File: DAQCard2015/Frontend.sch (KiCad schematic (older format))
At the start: 12 parts, among them P7 CONN_02X20_Double, U1 RJ45x8, U2 AD5628

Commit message: Adds APC128 connections and voltage supplies
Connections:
- net ADC_SCLK is gone; now on net SPI_SCLK: U2.16 (SCLK)
- net ADC_SDIO is gone; now on net SPI_SDIO: U2.15 (DIN)
- net Aref renamed Aref_A
- net Aref_A: no longer P7.74 (P34)
- net RBO1 renamed RBO_A1
- net RBO2 renamed RBO_A2
- net RBO3 renamed RBO_A3
- net RBO4 renamed RBO_A4
- net RBO5 renamed RBO_B1
- net RBO6 renamed RBO_B2
- net RBO7 renamed RBO_B3
- net RBO8 renamed RBO_B4
- net RG renamed RG_A
- net RG_A: no longer P7.56 (P16)
- net Vana renamed Vana_A
- net Vana_A: no longer P7.44 (P4), P7.45 (P5)
- new net Aref_B: P7.74 (P34)
- new net RG_B: P7.56 (P16)
- new net Vana_B: P7.44 (P4), P7.45 (P5)
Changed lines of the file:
@@
 	1    0    0    -1
 $EndComp
-Text GLabel 19750 4150 1    60   Input ~ 0
+Text GLabel 19750 4150 1    40   Input ~ 0
 GND
 Wire Wire Line
@@
 Wire Wire Line
 	19400 4650 19900 4650
-Text GLabel 19400 4650 0    60   Input ~ 0
+Text GLabel 19400 4650 0    40   Input ~ 0
 3V3dig
 Wire Wire Line
@@
 F28 "Vocm" I T 7600 3250 60
 $EndSheet
-Text HLabel 21000 4550 2    60   Input ~ 0
-ADC_SDIO
-Text HLabel 21000 4450 2    60   Input ~ 0
-ADC_SCLK
 $Sheet
 S 3750 7050 3400 1050
@@
 Text GLabel 3200 7700 1    40   Input ~ 0
 ADC_CLK-
-Text GLabel 19550 4550 1    60   Input ~ 0
+Text GLabel 19550 4550 1    40   Input ~ 0
 RNGDAC_CSB
 Text GLabel 7700 10350 2    40   Input ~ 0
-Vana
+Vana_A
 Text GLabel 7700 10450 2    40   Input ~ 0
 Vdig
@@
 CS
 Text GLabel 7700 10950 2    40   Input ~ 0
-RG
+RG_A
 Text GLabel 7700 11050 2    40   Input ~ 0
 IS2
@@
 SEB
 Text GLabel 7700 11550 2    40   Input ~ 0
-RBO1
+RBO_A1
 Text GLabel 7700 11650 2    40   Input ~ 0
-RBO3
+RBO_A3
 Text GLabel 7700 11750 2    40   Input ~ 0
 RPHI2
 Text GLabel 7700 11850 2    40   Input ~ 0
-Aref
+Aref_A
 Text GLabel 7700 10650 2    40   Input ~ 0
 5Vdig
@@
 RPHI1
 Text GLabel 7200 11750 0    40   Input ~ 0
-RBO4
+RBO_A4
 Text GLabel 7200 11650 0    40   Input ~ 0
-RBO2
+RBO_A2
 Text GLabel 7200 11450 0    40   Input ~ 0
 SBI
@@
 Vdig
 Text GLabel 7200 10450 0    40   Input ~ 0
-Vana
+Vana_A
 Text GLabel 7200 10250 0    40   Input ~ 0
 Vbias
@@
 RPHI1
 Text GLabel 8250 11750 0    40   Input ~ 0
-RBO8
+RBO_B4
 Text GLabel 8250 11650 0    40   Input ~ 0
-RBO6
+RBO_B2
 Text GLabel 8250 11450 0    40   Input ~ 0
 SBI
@@
 Vdig
 Text GLabel 8250 10450 0    40   Input ~ 0
-Vana
+Vana_B
 Text GLabel 8250 10250 0    40   Input ~ 0
 Vbias
@@
 SDA
 Text GLabel 8750 10350 2    40   Input ~ 0
-Vana
+Vana_B
 Text GLabel 8750 10450 2    40   Input ~ 0
 Vdig
@@
 CS
 Text GLabel 8750 10950 2    40   Input ~ 0
-RG
+RG_B
 Text GLabel 8750 11050 2    40   Input ~ 0
 IS2
@@
 SEB
 Text GLabel 8750 11550 2    40   Input ~ 0
-RBO5
+RBO_B1
 Text GLabel 8750 11650 2    40   Input ~ 0
-RBO7
+RBO_B3
 Text GLabel 8750 11750 2    40   Input ~ 0
 RPHI2
 Text GLabel 8750 11850 2    40   Input ~ 0
-Aref
+Aref_B
 Text GLabel 8750 10650 2    40   Input ~ 0
 5Vdig
 Text GLabel 8750 12050 2    40   Input ~ 0
 SCL
+Text GLabel 21000 4450 2    40   Input ~ 0
+SPI_SCLK
+Text GLabel 21000 4550 2    40   Input ~ 0
+SPI_SDIO
 $EndSCHEMATC

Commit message: Update to DAQ Board including adding an JTAG header and hooking up external clock and trigger
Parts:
- added C59, C61, C62, C63: 10uF, Capacitors_SMD:C_0805, symbol C
- added C78: .1uF, Capacitors_SMD:C_0603, symbol C
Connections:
- net 3V3ana: now also C59.1, C61.1, C62.1, C63.1
- net 3V3dig: now also C78.1
- net GND: now also C59.2, C61.2, C62.2, C63.2, C78.2
- net Vocm: no longer P7.48 (P8), P7.49 (P9), P7.8 (P8), P7.9 (P9)
- net Vdig renamed 2V5dig
- new net Vocm_tel: P7.48 (P8), P7.49 (P9), P7.8 (P8), P7.9 (P9)
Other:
- note added: "Amplifier Decoupling Caps"
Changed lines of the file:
@@
 	1    0    0    -1
 $EndComp
-Text GLabel 19750 4150 1    40   Input ~ 0
+Text GLabel 19750 4050 1    40   Input ~ 0
 GND
 Wire Wire Line
-	19900 4550 19550 4550
+	19900 4550 19600 4550
 Wire Wire Line
 	19750 4450 19900 4450
 Wire Wire Line
-	19750 4150 19750 4450
+	19750 4050 19750 4450
 Wire Wire Line
 	21000 4650 21500 4650
 Wire Wire Line
-	21500 5500 21500 4200
-Wire Wire Line
-	21500 4200 19750 4200
-Connection ~ 19750 4200
-Wire Wire Line
-	19400 4650 19900 4650
-Text GLabel 19400 4650 0    40   Input ~ 0
+	21500 4100 21500 5500
+Connection ~ 19750 4100
+Wire Wire Line
+	19250 4650 19900 4650
+Text GLabel 19250 4650 0    40   Input ~ 0
 3V3dig
 Wire Wire Line
@@
 $EndComp
 Wire Wire Line
-	20300 5500 21500 5500
+	21500 5500 20300 5500
 Connection ~ 21500 5150
 $Comp
@@
 Text GLabel 3200 7700 1    40   Input ~ 0
 ADC_CLK-
-Text GLabel 19550 4550 1    40   Input ~ 0
+Text GLabel 19600 4550 1    40   Input ~ 0
 RNGDAC_CSB
 Text GLabel 7700 10350 2    40   Input ~ 0
 Vana_A
 Text GLabel 7700 10450 2    40   Input ~ 0
-Vdig
+2V5dig
 Text GLabel 7700 10550 2    40   Input ~ 0
-Vocm
+Vocm_tel
 Text GLabel 7700 10750 2    40   Input ~ 0
 RBI
@@
 5Vdig
 Text GLabel 7200 10650 0    40   Input ~ 0
-Vocm
+Vocm_tel
 Text GLabel 7200 10550 0    40   Input ~ 0
-Vdig
+2V5dig
 Text GLabel 7200 10450 0    40   Input ~ 0
 Vana_A
@@
 5Vdig
 Text GLabel 8250 10650 0    40   Input ~ 0
-Vocm
+Vocm_tel
 Text GLabel 8250 10550 0    40   Input ~ 0
-Vdig
+2V5dig
 Text GLabel 8250 10450 0    40   Input ~ 0
 Vana_B
@@
 Vana_B
 Text GLabel 8750 10450 2    40   Input ~ 0
-Vdig
+2V5dig
 Text GLabel 8750 10550 2    40   Input ~ 0
-Vocm
+Vocm_tel
 Text GLabel 8750 10750 2    40   Input ~ 0
 RBI
@@
 Text GLabel 21000 4550 2    40   Input ~ 0
 SPI_SDIO
+$Comp
+L C C63
+U 1 1 5605A63E
+P 1900 5100
+F 0 "C63" H 1925 5200 50  0000 L CNN
+F 1 "10uF" H 1925 5000 50  0000 L CNN
+F 2 "Capacitors_SMD:C_0805" H 1938 4950 30  0001 C CNN
+F 3 "" H 1900 5100 60  0000 C CNN
+	1    1900 5100
+	1    0    0    -1
+$EndComp
+$Comp
+L C C62
+U 1 1 5605ACDA
+P 1700 5100
+F 0 "C62" H 1725 5200 50  0000 L CNN
+F 1 "10uF" H 1725 5000 50  0000 L CNN
+F 2 "Capacitors_SMD:C_0805" H 1738 4950 30  0001 C CNN
+F 3 "" H 1700 5100 60  0000 C CNN
+	1    1700 5100
+	1    0    0    -1
+$EndComp
+$Comp
+L C C61
+U 1 1 5605AD5D
+P 1500 5100
+F 0 "C61" H 1525 5200 50  0000 L CNN
+F 1 "10uF" H 1525 5000 50  0000 L CNN
+F 2 "Capacitors_SMD:C_0805" H 1538 4950 30  0001 C CNN
+F 3 "" H 1500 5100 60  0000 C CNN
+	1    1500 5100
+	1    0    0    -1
+$EndComp
+$Comp
+L C C59
+U 1 1 5605ADEB
+P 1300 5100
+F 0 "C59" H 1325 5200 50  0000 L CNN
+F 1 "10uF" H 1325 5000 50  0000 L CNN
+F 2 "Capacitors_SMD:C_0805" H 1338 4950 30  0001 C CNN
+F 3 "" H 1300 5100 60  0000 C CNN
+	1    1300 5100
+	1    0    0    -1
+$EndComp
+Wire Wire Line
+	1900 4900 1900 4950
+Wire Wire Line
+	1300 4900 2100 4900
+Wire Wire Line
+	1700 4950 1700 4900
+Connection ~ 1900 4900
+Wire Wire Line
+	1500 4950 1500 4900
+Connection ~ 1700 4900
+Wire Wire Line
+	1300 4950 1300 4900
+Connection ~ 1500 4900
+Wire Wire Line
+	1900 5300 1900 5250
+Wire Wire Line
+	1300 5300 2100 5300
+Wire Wire Line
+	1700 5250 1700 5300
+Connection ~ 1900 5300
+Wire Wire Line
+	1500 5250 1500 5300
+Connection ~ 1700 5300
+Wire Wire Line
+	1300 5250 1300 5300
+Connection ~ 1500 5300
+Text GLabel 2100 4900 2    40   Input ~ 0
+3V3ana
+Text GLabel 2100 5300 2    40   Input ~ 0
+GND
+Text Notes 1200 5450 0    60   ~ 0
+Amplifier Decoupling Caps
+$Comp
+L C C78
+U 1 1 560B787A
+P 19350 4400
+F 0 "C78" H 19375 4500 50  0000 L CNN
+F 1 ".1uF" H 19375 4300 50  0000 L CNN
+F 2 "Capacitors_SMD:C_0603" H 19388 4250 30  0001 C CNN
+F 3 "" H 19350 4400 60  0000 C CNN
+	1    19350 4400
+	-1   0    0    1
+$EndComp
+Wire Wire Line
+	19350 4250 19350 4100
+Wire Wire Line
+	19350 4550 19350 4650
+Connection ~ 19350 4650
+Wire Wire Line
+	19350 4100 21500 4100
 $EndSCHEMATC

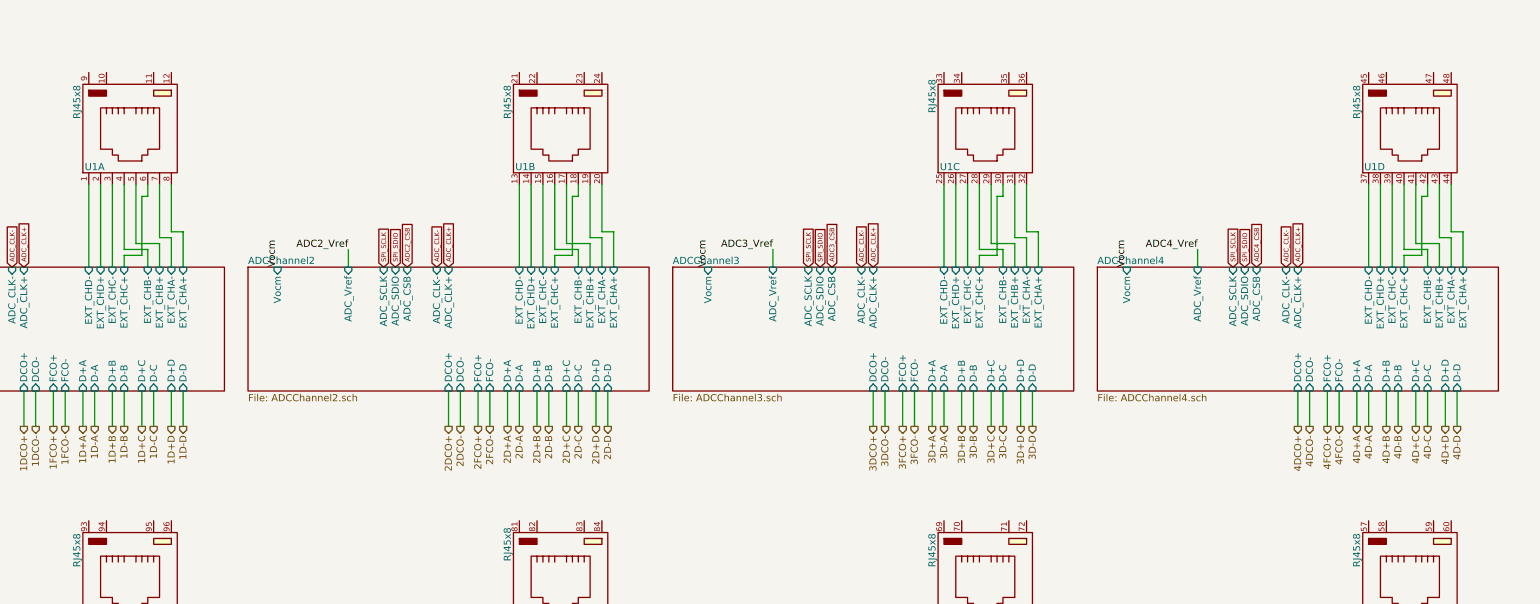
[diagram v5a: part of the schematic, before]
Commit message: Update V1.0 of DAQ Board Includes LED Driver for RJ45 Port, repositioning of JTAG
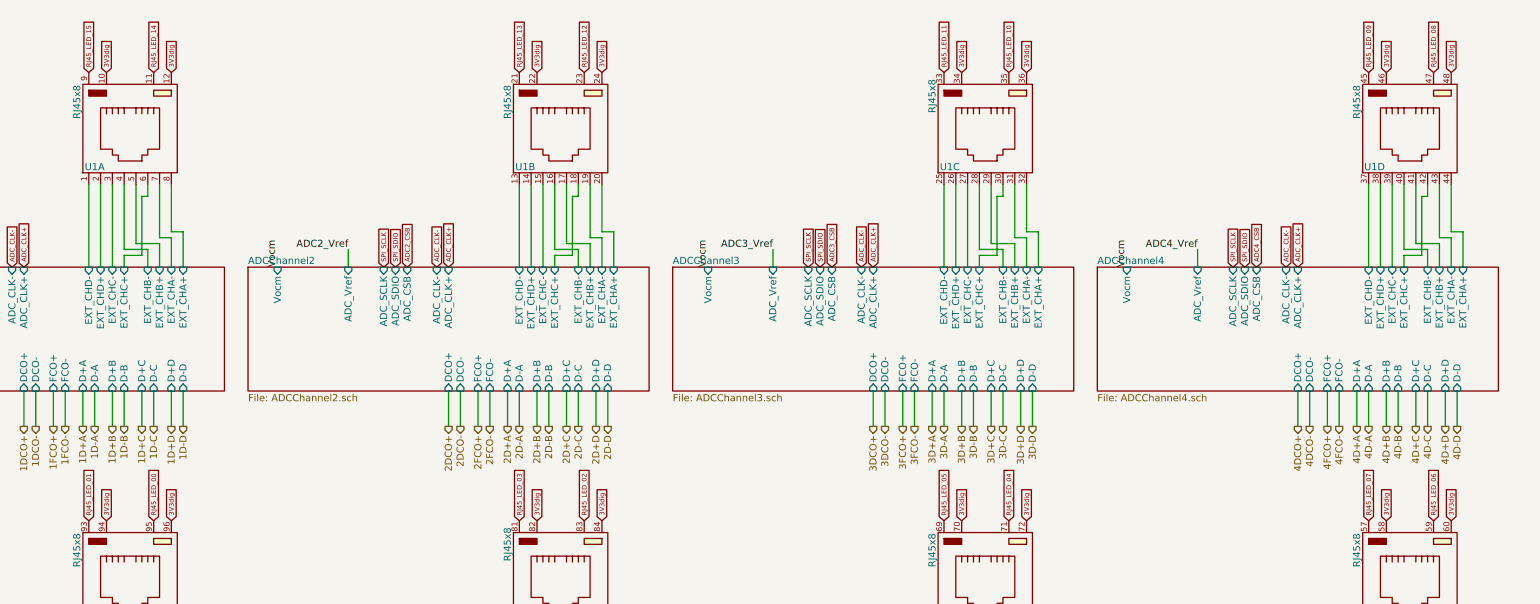
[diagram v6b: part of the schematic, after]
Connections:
- net 3V3dig: now also U1.10, U1.12, U1.22, U1.24, U1.34, U1.36, U1.46, U1.48, U1.58, U1.60, U1.70, U1.72, U1.82, U1.84, U1.94, U1.96
- net RJ45_LED_14: now reaches U1.11
- net RJ45_LED_15: now reaches U1.9
- net RJ45_LED_11: now reaches U1.33
- net RJ45_LED_10: now reaches U1.35
- net RJ45_LED_07: now reaches U1.57
- net RJ45_LED_06: now reaches U1.59
- net RJ45_LED_03: now reaches U1.81
- net RJ45_LED_02: now reaches U1.83
- net RJ45_LED_01: now reaches U1.93
- net RJ45_LED_00: now reaches U1.95
- net RJ45_LED_05: now reaches U1.69
- net RJ45_LED_04: now reaches U1.71
- net RJ45_LED_09: now reaches U1.45
- net RJ45_LED_08: now reaches U1.47
- net RJ45_LED_13: now reaches U1.21
- net RJ45_LED_12: now reaches U1.23
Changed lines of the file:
@@
 Wire Wire Line
 	19350 4100 21500 4100
+Text GLabel 6150 1600 1    40   Input ~ 0
+3V3dig
+Text GLabel 6700 1600 1    40   Input ~ 0
+3V3dig
+Text GLabel 6000 1600 1    40   Input ~ 0
+RJ45_LED_15
+Text GLabel 6550 1600 1    40   Input ~ 0
+RJ45_LED_14
+Text GLabel 9800 1600 1    40   Input ~ 0
+3V3dig
+Text GLabel 10350 1600 1    40   Input ~ 0
+3V3dig
+Text GLabel 9650 1600 1    40   Input ~ 0
+RJ45_LED_13
+Text GLabel 10200 1600 1    40   Input ~ 0
+RJ45_LED_12
+Text GLabel 13400 1600 1    40   Input ~ 0
+3V3dig
+Text GLabel 13950 1600 1    40   Input ~ 0
+3V3dig
+Text GLabel 13250 1600 1    40   Input ~ 0
+RJ45_LED_11
+Text GLabel 13800 1600 1    40   Input ~ 0
+RJ45_LED_10
+Text GLabel 17000 1600 1    40   Input ~ 0
+3V3dig
+Text GLabel 17550 1600 1    40   Input ~ 0
+3V3dig
+Text GLabel 16850 1600 1    40   Input ~ 0
+RJ45_LED_09
+Text GLabel 17400 1600 1    40   Input ~ 0
+RJ45_LED_08
+Text GLabel 6150 5400 1    40   Input ~ 0
+3V3dig
+Text GLabel 6700 5400 1    40   Input ~ 0
+3V3dig
+Text GLabel 6550 5400 1    40   Input ~ 0
+RJ45_LED_00
+Text GLabel 6000 5400 1    40   Input ~ 0
+RJ45_LED_01
+Text GLabel 9800 5400 1    40   Input ~ 0
+3V3dig
+Text GLabel 10350 5400 1    40   Input ~ 0
+3V3dig
+Text GLabel 9650 5400 1    40   Input ~ 0
+RJ45_LED_03
+Text GLabel 10200 5400 1    40   Input ~ 0
+RJ45_LED_02
+Text GLabel 13400 5400 1    40   Input ~ 0
+3V3dig
+Text GLabel 13950 5400 1    40   Input ~ 0
+3V3dig
+Text GLabel 13250 5400 1    40   Input ~ 0
+RJ45_LED_05
+Text GLabel 13800 5400 1    40   Input ~ 0
+RJ45_LED_04
+Text GLabel 17000 5400 1    40   Input ~ 0
+3V3dig
+Text GLabel 17550 5400 1    40   Input ~ 0
+3V3dig
+Text GLabel 16850 5400 1    40   Input ~ 0
+RJ45_LED_07
+Text GLabel 17400 5400 1    40   Input ~ 0
+RJ45_LED_06
 $EndSCHEMATC

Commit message: Adds digipart field to all parts that is now used in automatic generation of BOM(see DAQCard2015.html)
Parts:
- C1, C59, C61, C62, C63: digipart (none) -> 445-11464-1-ND
- C2, C4, C78: digipart (none) -> 445-1316-1-ND
- C3: digipart (none) -> 445-1311-1-ND
- P7: digipart (none) -> 3M15351-ND
- R1: digipart (none) -> P2.70KHCT-ND
- R2, R5: digipart (none) -> P1.00KHCT-ND
- R3: digipart (none) -> P100HCT-ND
- R4: digipart (none) -> P2.40KHCT-ND
- U1: digipart (none) -> A119312-ND
- U2: digipart (none) -> AD5628ARUZ-2-ND
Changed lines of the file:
@@
 F 2 "Resistors_SMD:R_0603" V 3080 7850 30  0001 C CNN
 F 3 "" H 3150 7850 30  0000 C CNN
+F 4 "P100HCT-ND" V 3150 7850 60  0001 C CNN "digipart"
 	1    3150 7850
 	0    -1   -1   0
@@
 F 2 "extras:TSSOP-16_4.4x5mm_Pitch0.65mm" H 20650 4950 60  0001 C CNN
 F 3 "" H 20650 4950 60  0000 C CNN
+F 4 "AD5628ARUZ-2-ND" H 20450 4800 60  0001 C CNN "digipart"
 	1    20450 4800
 	1    0    0    -1
@@
 F 2 "Resistors_SMD:R_0603" V 19580 5500 30  0001 C CNN
 F 3 "" H 19650 5500 30  0000 C CNN
+F 4 "P2.40KHCT-ND" V 19650 5500 60  0001 C CNN "digipart"
 	1    19650 5500
 	0    1    1    0
@@
 F 2 "Resistors_SMD:R_0603" V 20080 5500 30  0001 C CNN
 F 3 "" H 20150 5500 30  0000 C CNN
+F 4 "P1.00KHCT-ND" V 20150 5500 60  0001 C CNN "digipart"
 	1    20150 5500
 	0    1    1    0
@@
 F 2 "Capacitors_SMD:C_0603" H 20188 5550 30  0001 C CNN
 F 3 "" H 20150 5700 60  0000 C CNN
+F 4 "445-1316-1-ND" H 20150 5700 60  0001 C CNN "digipart"
 	1    20150 5700
 	0    -1   -1   0
@@
 F 2 "extras:TE_406967-3" H 6200 2350 60  0001 C CNN
 F 3 "" H 6200 2350 60  0000 C CNN
+F 4 "A119312-ND" H 6200 2350 60  0001 C CNN "digipart"
 	1    6200 2350
 	1    0    0    -1
@@
 F 2 "Capacitors_SMD:C_0805" H 1288 3750 30  0001 C CNN
 F 3 "" H 1250 3900 60  0000 C CNN
+F 4 "445-11464-1-ND" H 1250 3900 60  0001 C CNN "digipart"
 	1    1250 3900
 	1    0    0    -1
@@
 F 2 "Capacitors_SMD:C_0603" H 1488 3750 30  0001 C CNN
 F 3 "" H 1450 3900 60  0000 C CNN
+F 4 "445-1316-1-ND" H 1450 3900 60  0001 C CNN "digipart"
 	1    1450 3900
 	1    0    0    -1
@@
 F 2 "Capacitors_SMD:C_0603" H 2038 3900 30  0001 C CNN
 F 3 "" H 2000 4050 60  0000 C CNN
+F 4 "445-1311-1-ND" H 2000 4050 60  0001 C CNN "digipart"
 	1    2000 4050
 	1    0    0    -1
@@
 F 2 "Resistors_SMD:R_0603" V 1680 3650 30  0001 C CNN
 F 3 "" H 1750 3650 30  0000 C CNN
+F 4 "P2.70KHCT-ND" V 1750 3650 60  0001 C CNN "digipart"
 	1    1750 3650
 	1    0    0    -1
@@
 F 2 "Resistors_SMD:R_0603" V 1680 4050 30  0001 C CNN
 F 3 "" H 1750 4050 30  0000 C CNN
+F 4 "P1.00KHCT-ND" V 1750 4050 60  0001 C CNN "digipart"
 	1    1750 4050
 	1    0    0    -1
@@
 F 2 "extras:N3432-D302RB" H 7450 10250 60  0001 C CNN
 F 3 "" H 7450 10250 60  0000 C CNN
+F 4 "3M15351-ND" H 7450 11200 60  0001 C CNN "digipart"
 	1    7450 11200
 	1    0    0    -1
@@
 F 2 "Capacitors_SMD:C_0805" H 1938 4950 30  0001 C CNN
 F 3 "" H 1900 5100 60  0000 C CNN
+F 4 "445-11464-1-ND" H 1900 5100 60  0001 C CNN "digipart"
 	1    1900 5100
 	1    0    0    -1
@@
 F 2 "Capacitors_SMD:C_0805" H 1738 4950 30  0001 C CNN
 F 3 "" H 1700 5100 60  0000 C CNN
+F 4 "445-11464-1-ND" H 1700 5100 60  0001 C CNN "digipart"
 	1    1700 5100
 	1    0    0    -1
@@
 F 2 "Capacitors_SMD:C_0805" H 1538 4950 30  0001 C CNN
 F 3 "" H 1500 5100 60  0000 C CNN
+F 4 "445-11464-1-ND" H 1500 5100 60  0001 C CNN "digipart"
 	1    1500 5100
 	1    0    0    -1
@@
 F 2 "Capacitors_SMD:C_0805" H 1338 4950 30  0001 C CNN
 F 3 "" H 1300 5100 60  0000 C CNN
+F 4 "445-11464-1-ND" H 1300 5100 60  0001 C CNN "digipart"
 	1    1300 5100
 	1    0    0    -1
@@
 F 2 "Capacitors_SMD:C_0603" H 19388 4250 30  0001 C CNN
 F 3 "" H 19350 4400 60  0000 C CNN
+F 4 "445-1316-1-ND" H 19350 4400 60  0001 C CNN "digipart"
 	1    19350 4400
 	-1   0    0    1

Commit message: annotates parts for new build-management tool
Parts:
- C1, C59, C61, C62, C63: Digikey (none) -> 445-11464-1-ND; digipart 445-11464-1-ND -> (none)
- C2, C4, C78: Digikey (none) -> 445-1316-1-ND; digipart 445-1316-1-ND -> (none)
- C3: Digikey (none) -> 445-1311-1-ND; digipart 445-1311-1-ND -> (none)
- P7: Digikey (none) -> 3M15351-ND; digipart 3M15351-ND -> (none)
- R1: Digikey (none) -> P2.70KHCT-ND; digipart P2.70KHCT-ND -> (none)
- R2, R5: Digikey (none) -> P1.00KHCT-ND; digipart P1.00KHCT-ND -> (none)
- R3: Digikey (none) -> P100HCT-ND; digipart P100HCT-ND -> (none)
- R4: Digikey (none) -> P2.40KHCT-ND; digipart P2.40KHCT-ND -> (none)
- U1: Digikey (none) -> A119312-ND; digipart A119312-ND -> (none)
- U2: Digikey (none) -> AD5628ARUZ-2-ND; digipart AD5628ARUZ-2-ND -> (none)
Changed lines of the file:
@@
 EESchema Schematic File Version 2
+LIBS:DAQCard2015-rescue
 LIBS:power
 LIBS:device
@@
 F 2 "Resistors_SMD:R_0603" V 3080 7850 30  0001 C CNN
 F 3 "" H 3150 7850 30  0000 C CNN
-F 4 "P100HCT-ND" V 3150 7850 60  0001 C CNN "digipart"
+F 4 "P100HCT-ND" V 3150 7850 60  0001 C CNN "Digikey"
 	1    3150 7850
 	0    -1   -1   0
@@
 F 2 "extras:TSSOP-16_4.4x5mm_Pitch0.65mm" H 20650 4950 60  0001 C CNN
 F 3 "" H 20650 4950 60  0000 C CNN
-F 4 "AD5628ARUZ-2-ND" H 20450 4800 60  0001 C CNN "digipart"
+F 4 "AD5628ARUZ-2-ND" H 20450 4800 60  0001 C CNN "Digikey"
 	1    20450 4800
 	1    0    0    -1
@@
 F 2 "Resistors_SMD:R_0603" V 19580 5500 30  0001 C CNN
 F 3 "" H 19650 5500 30  0000 C CNN
-F 4 "P2.40KHCT-ND" V 19650 5500 60  0001 C CNN "digipart"
+F 4 "P2.40KHCT-ND" V 19650 5500 60  0001 C CNN "Digikey"
 	1    19650 5500
 	0    1    1    0
@@
 F 2 "Resistors_SMD:R_0603" V 20080 5500 30  0001 C CNN
 F 3 "" H 20150 5500 30  0000 C CNN
-F 4 "P1.00KHCT-ND" V 20150 5500 60  0001 C CNN "digipart"
+F 4 "P1.00KHCT-ND" V 20150 5500 60  0001 C CNN "Digikey"
 	1    20150 5500
 	0    1    1    0
@@
 F 2 "Capacitors_SMD:C_0603" H 20188 5550 30  0001 C CNN
 F 3 "" H 20150 5700 60  0000 C CNN
-F 4 "445-1316-1-ND" H 20150 5700 60  0001 C CNN "digipart"
+F 4 "445-1316-1-ND" H 20150 5700 60  0001 C CNN "Digikey"
 	1    20150 5700
 	0    -1   -1   0
@@
 F 2 "extras:TE_406967-3" H 6200 2350 60  0001 C CNN
 F 3 "" H 6200 2350 60  0000 C CNN
-F 4 "A119312-ND" H 6200 2350 60  0001 C CNN "digipart"
+F 4 "A119312-ND" H 6200 2350 60  0001 C CNN "Digikey"
 	1    6200 2350
 	1    0    0    -1
@@
 F 2 "Capacitors_SMD:C_0805" H 1288 3750 30  0001 C CNN
 F 3 "" H 1250 3900 60  0000 C CNN
-F 4 "445-11464-1-ND" H 1250 3900 60  0001 C CNN "digipart"
+F 4 "445-11464-1-ND" H 1250 3900 60  0001 C CNN "Digikey"
 	1    1250 3900
 	1    0    0    -1
@@
 F 2 "Capacitors_SMD:C_0603" H 1488 3750 30  0001 C CNN
 F 3 "" H 1450 3900 60  0000 C CNN
-F 4 "445-1316-1-ND" H 1450 3900 60  0001 C CNN "digipart"
+F 4 "445-1316-1-ND" H 1450 3900 60  0001 C CNN "Digikey"
 	1    1450 3900
 	1    0    0    -1
@@
 F 2 "Capacitors_SMD:C_0603" H 2038 3900 30  0001 C CNN
 F 3 "" H 2000 4050 60  0000 C CNN
-F 4 "445-1311-1-ND" H 2000 4050 60  0001 C CNN "digipart"
+F 4 "445-1311-1-ND" H 2000 4050 60  0001 C CNN "Digikey"
 	1    2000 4050
 	1    0    0    -1
@@
 F 2 "Resistors_SMD:R_0603" V 1680 3650 30  0001 C CNN
 F 3 "" H 1750 3650 30  0000 C CNN
-F 4 "P2.70KHCT-ND" V 1750 3650 60  0001 C CNN "digipart"
+F 4 "P2.70KHCT-ND" V 1750 3650 60  0001 C CNN "Digikey"
 	1    1750 3650
 	1    0    0    -1
@@
 F 2 "Resistors_SMD:R_0603" V 1680 4050 30  0001 C CNN
 F 3 "" H 1750 4050 30  0000 C CNN
-F 4 "P1.00KHCT-ND" V 1750 4050 60  0001 C CNN "digipart"
+F 4 "P1.00KHCT-ND" V 1750 4050 60  0001 C CNN "Digikey"
 	1    1750 4050
 	1    0    0    -1
@@
 F 2 "extras:N3432-D302RB" H 7450 10250 60  0001 C CNN
 F 3 "" H 7450 10250 60  0000 C CNN
-F 4 "3M15351-ND" H 7450 11200 60  0001 C CNN "digipart"
+F 4 "3M15351-ND" H 7450 11200 60  0001 C CNN "Digikey"
 	1    7450 11200
 	1    0    0    -1
@@
 F 2 "Capacitors_SMD:C_0805" H 1938 4950 30  0001 C CNN
 F 3 "" H 1900 5100 60  0000 C CNN
-F 4 "445-11464-1-ND" H 1900 5100 60  0001 C CNN "digipart"
+F 4 "445-11464-1-ND" H 1900 5100 60  0001 C CNN "Digikey"
 	1    1900 5100
 	1    0    0    -1
@@
 F 2 "Capacitors_SMD:C_0805" H 1738 4950 30  0001 C CNN
 F 3 "" H 1700 5100 60  0000 C CNN
-F 4 "445-11464-1-ND" H 1700 5100 60  0001 C CNN "digipart"
+F 4 "445-11464-1-ND" H 1700 5100 60  0001 C CNN "Digikey"
 	1    1700 5100
 	1    0    0    -1
@@
 F 2 "Capacitors_SMD:C_0805" H 1538 4950 30  0001 C CNN
 F 3 "" H 1500 5100 60  0000 C CNN
-F 4 "445-11464-1-ND" H 1500 5100 60  0001 C CNN "digipart"
+F 4 "445-11464-1-ND" H 1500 5100 60  0001 C CNN "Digikey"
 	1    1500 5100
 	1    0    0    -1
@@
 F 2 "Capacitors_SMD:C_0805" H 1338 4950 30  0001 C CNN
 F 3 "" H 1300 5100 60  0000 C CNN
-F 4 "445-11464-1-ND" H 1300 5100 60  0001 C CNN "digipart"
+F 4 "445-11464-1-ND" H 1300 5100 60  0001 C CNN "Digikey"
 	1    1300 5100
 	1    0    0    -1
@@
 F 2 "Capacitors_SMD:C_0603" H 19388 4250 30  0001 C CNN
 F 3 "" H 19350 4400 60  0000 C CNN
-F 4 "445-1316-1-ND" H 19350 4400 60  0001 C CNN "digipart"
+F 4 "445-1316-1-ND" H 19350 4400 60  0001 C CNN "Digikey"
 	1    19350 4400
 	-1   0    0    1
